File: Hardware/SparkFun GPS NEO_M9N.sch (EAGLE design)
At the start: 50 parts, among them J13 U.FL, J2 Qwiic Right Angle, J4 Qwiic Right Angle, U1 U-BLOX_NEO-M9N, U2 3.3V

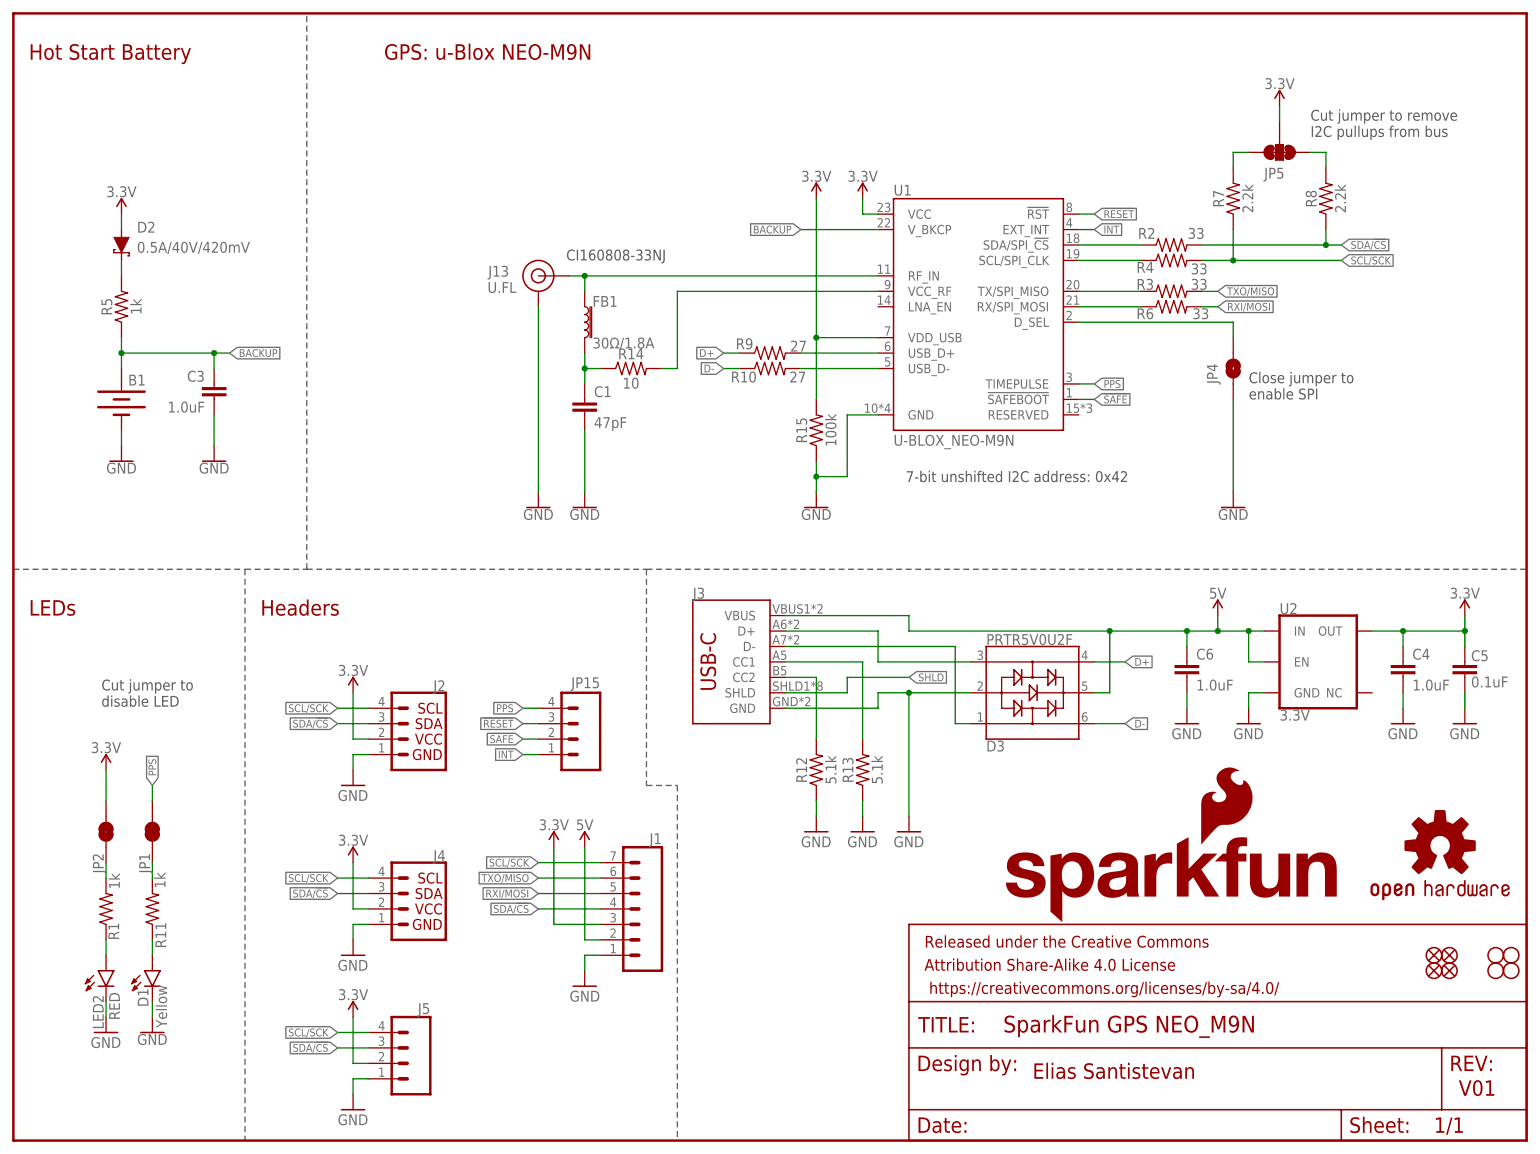
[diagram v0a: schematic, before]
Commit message: Updates the order of the info boxes in the schematic, adds 10k pullup to D_SEL
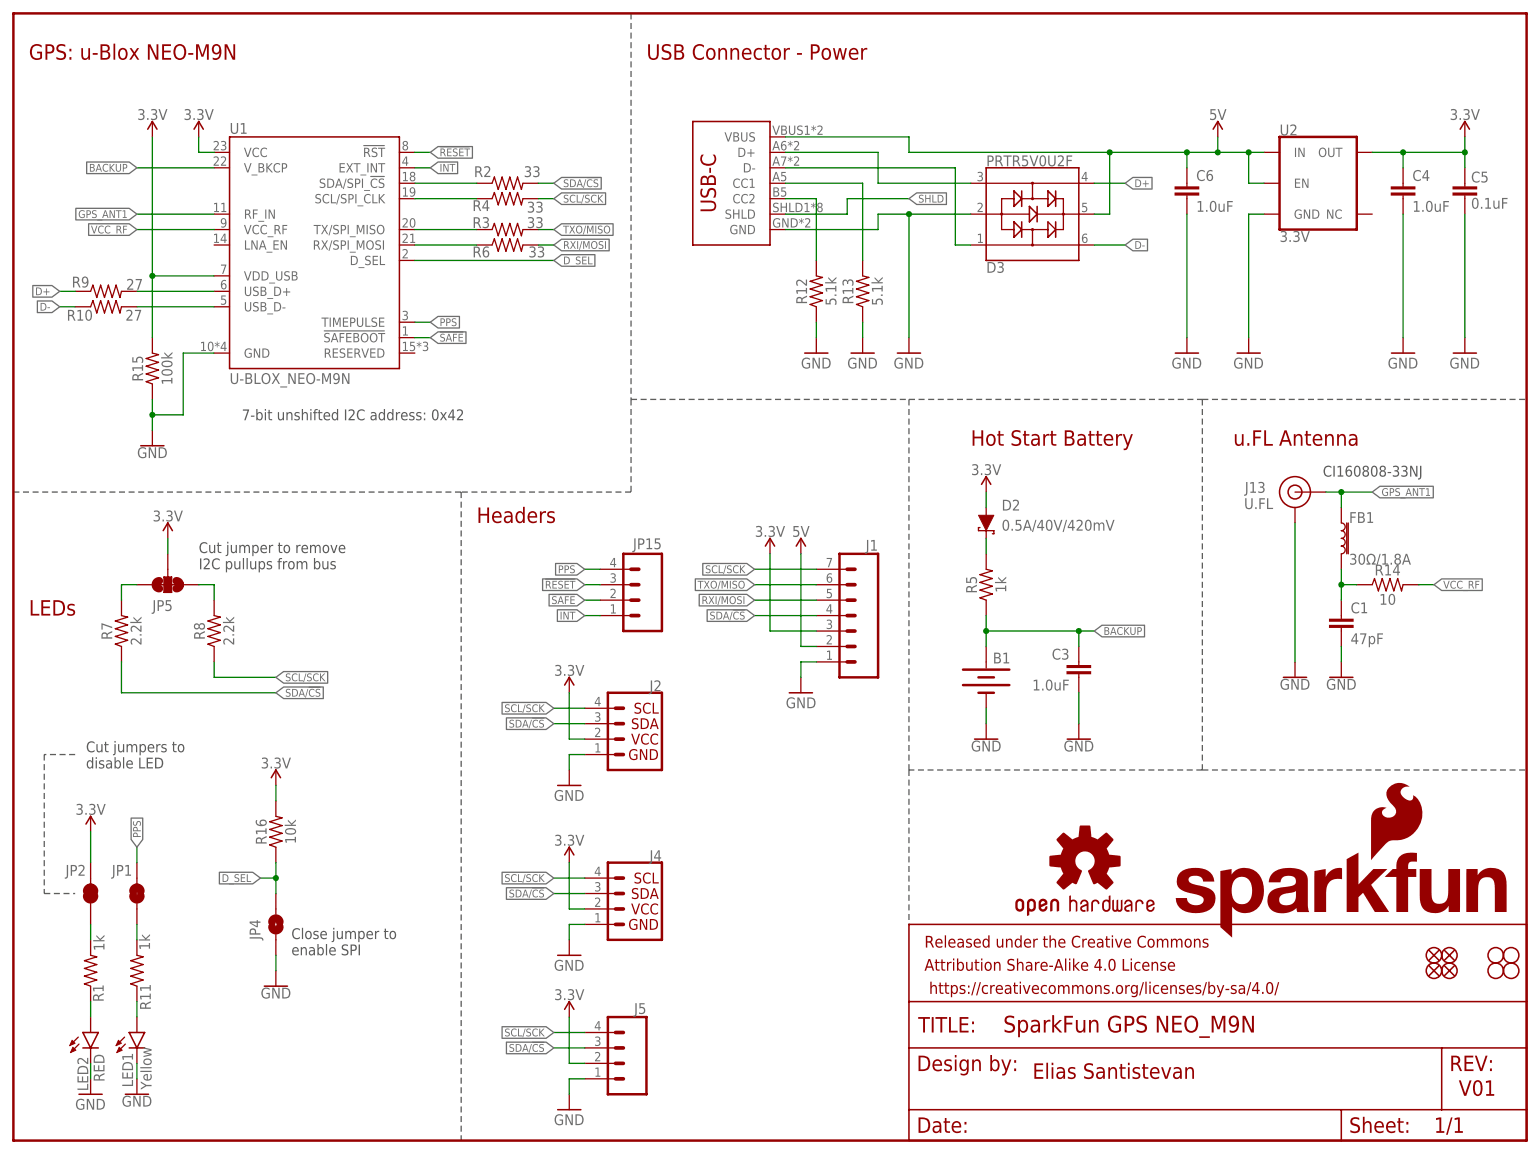
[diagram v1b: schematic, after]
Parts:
- removed D1: Yellow, SparkFun-LED:LED-YELLOW0603
- added LED1: Yellow, SparkFun-LED:LED-YELLOW0603
- added R16: 10k, SparkFun-Resistors:10KOHM-0402-1/16W-1%
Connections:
- net N$13 renamed VCC_RF
- net 3.3V: now also R16.2
- net D_SEL: now also R16.1
- net GND: now also LED1.C; no longer D1.C
- net N$2: now also LED1.A; no longer D1.A
- net SCL/SCK: now also R8.1; no longer R7.1
- net SDA/!CS: now also R7.1; no longer R8.1
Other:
- note added: "Cut jumpers to disable LED"
- note added: "USB Connector - Power"
- note added: "u.FL Antenna"
- note removed: "Cut jumper to disable LED"
- moved on the sheet: B1, C1, C3, C4, C5, C6, D2, D3, FB1, J1, J13, J2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

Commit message: Routes 10k pullup resistor, adds labels, fixes air wires
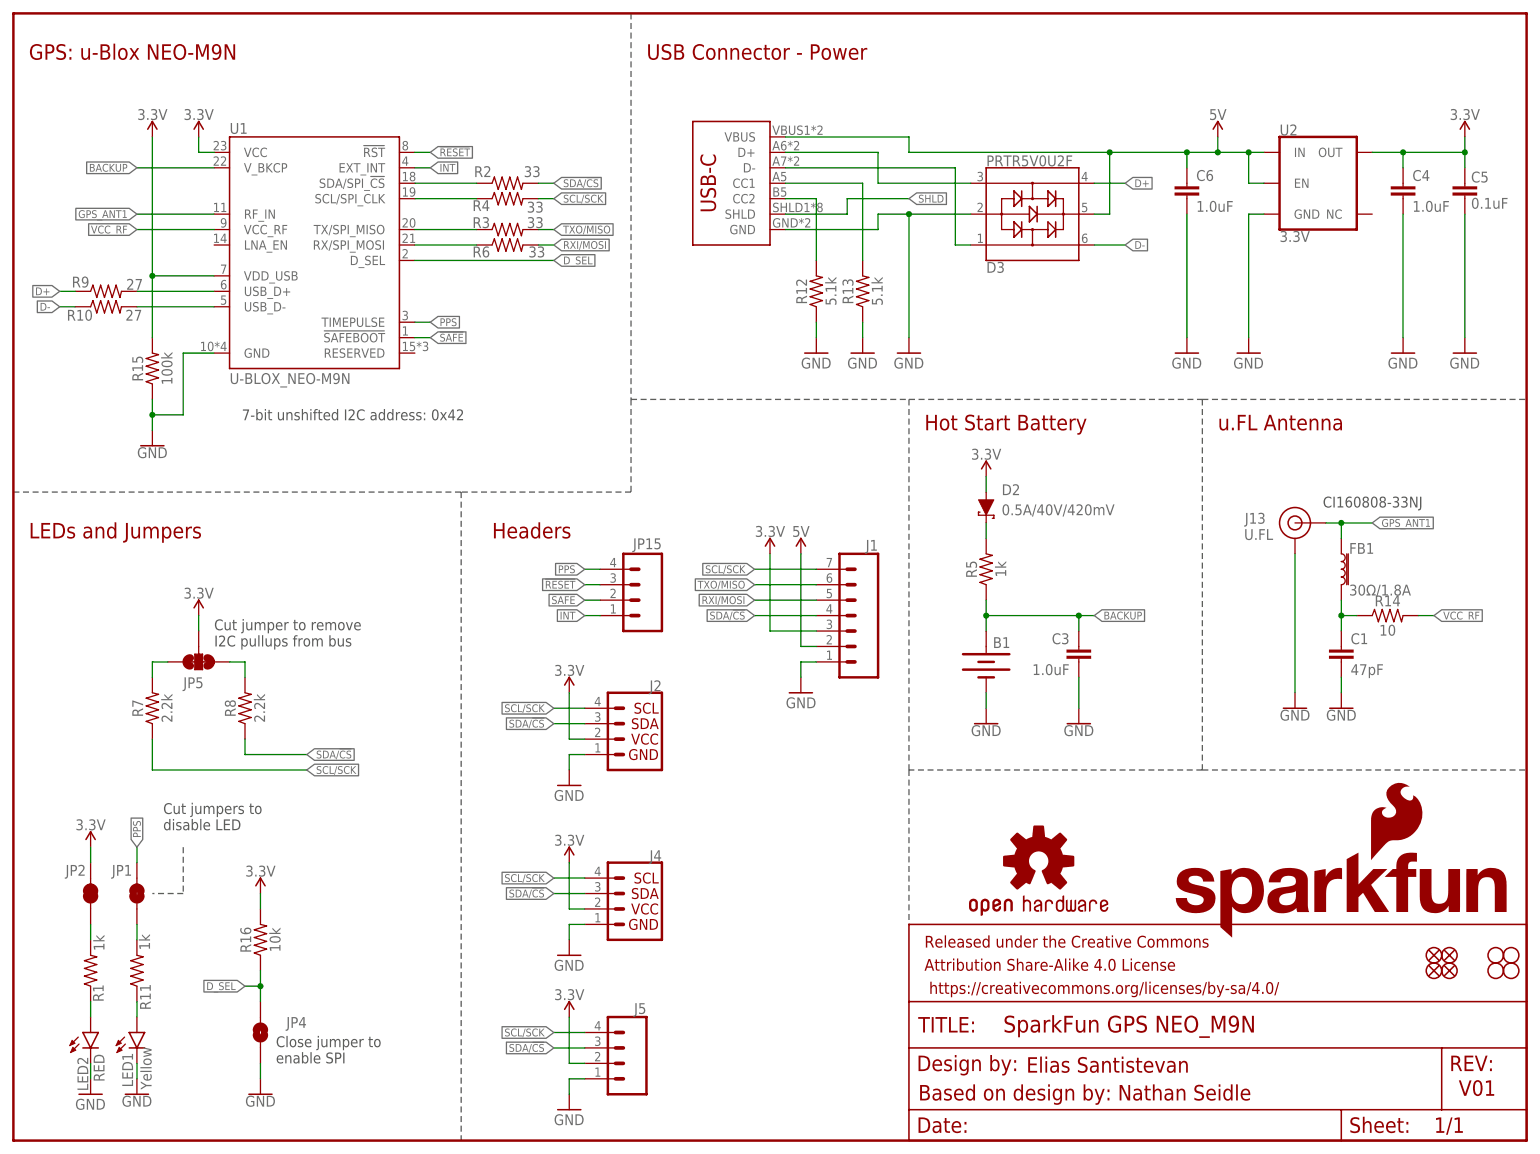
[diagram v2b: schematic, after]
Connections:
- net SCL/SCK: now also R7.1; no longer R8.1
- net SDA/!CS: now also R8.1; no longer R7.1
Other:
- note added: "Based on design by: Nathan Seidle"
- note added: "LEDs and Jumpers"
- note removed: "LEDs"
- moved on the sheet: B1, C1, C3, D2, FB1, J13, JP4, JP5, R14, R16, R5, R7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
